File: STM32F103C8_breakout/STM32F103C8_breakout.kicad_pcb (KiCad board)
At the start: 2 copper layers, 49 parts, among them J1 Conn1x1Pin-PA0_WKUP, J10 Conn1x1Pin-PA9, J11 Conn1x1Pin-PA10, J12 Conn1x1Pin-PA11, J13 Conn1x1Pin-PA12, J14 Conn1x1Pin-PA13, J15 Conn1x1Pin-PA14, J16 Conn1x1Pin-PA15, J17 Conn1x1Pin-PC13-TAMPER-RTC, J18 Conn1x1Pin-PC14-OSC32_IN, J19 Conn1x1Pin-PC15-OSC32_OUT, J2 Conn1x1Pin-PA1, J20 Conn1x1Pin-VBAT, J21 Conn1x1Pin-NRST, J22 BOOT0, J23 Conn1x1Pin-VDD, J24 Conn1x1Pin-VDDA, J25 Conn1x1Pin-PB15, J26 Conn1x1Pin-PB14, J27 Conn1x1Pin-PB13, J28 Conn1x1Pin-PB12, J29 Conn1x1Pin-PB11, J3 Conn1x1Pin-PA2, J30 Conn1x1Pin-PB10, J31 Conn1x1Pin-PB9, J32 Conn1x1Pin-PB8, J33 Conn1x1Pin-PB7, J34 Conn1x1Pin-PB6, J35 Conn1x1Pin-PB5, J36 Conn1x1Pin-PB4, J37 Conn1x1Pin-PB3, J38 Conn1x1Pin-PB2, J39 Conn1x1Pin-PB1, J4 Conn1x1Pin-PA3, J40 Conn1x1Pin-PB0, J41 Conn1x1Pin-PC0_OSC_IN, J42 Conn1x1Pin-PD1_OSC_OUT, J43 Conn1x1Pin-VSSA, J44 Conn1x1Pin-VSS, J5 Conn1x1Pin-PA4, J6 Conn1x1Pin-PA5, J7 Conn1x1Pin-PA6, J8 Conn1x1Pin-PA7, J9 Conn1x1Pin-PA8, U1 STM32F103C8T6

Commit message: Added to Schematics
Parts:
- removed J20: Conn1x1Pin-VBAT, Connector_PinHeader_2.54mm:PinHeader_1x01_P2.54mm_Horizontal
- removed J21: Conn1x1Pin-NRST, Connector_PinHeader_2.54mm:PinHeader_1x01_P2.54mm_Horizontal
- removed J22: BOOT0, Connector_PinHeader_2.54mm:PinHeader_1x01_P2.54mm_Horizontal
- removed J23 (x3): Conn1x1Pin-VDD, Connector_PinHeader_2.54mm:PinHeader_1x01_P2.54mm_Horizontal
- removed J24: Conn1x1Pin-VDDA, Connector_PinHeader_2.54mm:PinHeader_1x01_P2.54mm_Horizontal
- removed J41: Conn1x1Pin-PC0_OSC_IN, Connector_PinHeader_2.54mm:PinHeader_1x01_P2.54mm_Horizontal
- removed J42: Conn1x1Pin-PD1_OSC_OUT, Connector_PinHeader_2.54mm:PinHeader_1x01_P2.54mm_Horizontal
- removed J43: Conn1x1Pin-VSSA, Connector_PinHeader_2.54mm:PinHeader_1x01_P2.54mm_Horizontal
- removed J44 (x3): Conn1x1Pin-VSS, Connector_PinHeader_2.54mm:PinHeader_1x01_P2.54mm_Horizontal
- removed U1: STM32F103C8T6, STM32F103C8T6:QFP50P900X900X160-48N
- added C1: 1μF, Capacitor_SMD:C_0805_2012Metric_Pad1.18x1.45mm_HandSolder, F.Cu at (178.4, 50.0)
- added C2: 100nF, Capacitor_SMD:C_0805_2012Metric_Pad1.18x1.45mm_HandSolder, F.Cu at (178.4, 53.0)
- added C3: 100nF, Capacitor_SMD:C_0805_2012Metric_Pad1.18x1.45mm_HandSolder, F.Cu at (178.4, 56.0)
- added C4: 20pF, Capacitor_SMD:C_0805_2012Metric_Pad1.18x1.45mm_HandSolder, F.Cu at (178.4, 59.0)
- added C5: 20pF, Capacitor_SMD:C_0805_2012Metric_Pad1.18x1.45mm_HandSolder, F.Cu at (178.4, 62.0)
- added FB1: FerriteBead_Small, Inductor_SMD:L_0805_2012Metric_Pad1.05x1.20mm_HandSolder, F.Cu at (178.4, 79.6)
- added JLINK/SWD1: ~, Connector_IDC:IDC-Header_2x10_P2.54mm_Vertical, F.Cu at (239.2, 71.8)
- added R1: 10kΩ, Resistor_SMD:R_0805_2012Metric_Pad1.20x1.40mm_HandSolder, F.Cu at (178.3, 65.0)
- added R2: 10kΩ, Resistor_SMD:R_0805_2012Metric_Pad1.20x1.40mm_HandSolder, F.Cu at (178.3, 67.9)
- added R3: 10kΩ, Resistor_SMD:R_0805_2012Metric_Pad1.20x1.40mm_HandSolder, F.Cu at (178.3, 70.9)
- added R5: 10kΩ, Resistor_SMD:R_0805_2012Metric_Pad1.20x1.40mm_HandSolder, F.Cu at (178.3, 73.8)
- added R6: 400Ω, Resistor_SMD:R_0805_2012Metric_Pad1.20x1.40mm_HandSolder, F.Cu at (178.3, 76.8)
- added Y1: 6 MHz Crystal, Crystal:Crystal_SMD_HC49-SD_HandSoldering, F.Cu at (227.0, 61.5)
- moved J17 107.2 mm to (139.5, 69.1), turned to 0 degrees
- moved J18 99.9 mm to (139.5, 73.7), turned to 0 degrees
- moved J31 96.1 mm to (152.9, 55.4), turned to 0 degrees
- moved J19 92.7 mm to (139.5, 78.3), turned to 0 degrees
- moved J30 92.7 mm to (152.9, 50.8), turned to 0 degrees
- moved J1 90.9 mm to (126.2, 50.8), turned to 0 degrees
- moved J32 90.4 mm to (152.9, 59.9), turned to 0 degrees
- moved J2 85.1 mm to (126.2, 55.4), turned to 0 degrees
- moved J3 79.5 mm to (126.2, 59.9), turned to 0 degrees
- moved J33 79.5 mm to (152.9, 64.5), turned to 0 degrees
- moved J4 75.9 mm to (126.2, 64.5), turned to 0 degrees
- moved J28 75.1 mm to (139.5, 96.7), turned to 0 degrees
- moved J34 74.3 mm to (152.9, 69.1), turned to 0 degrees
- moved J5 72.1 mm to (126.2, 69.1), turned to 0 degrees
- moved J35 69.6 mm to (152.9, 73.7), turned to 0 degrees
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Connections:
- J14 pad 1: Net-(J14-Pin_1) -> /JTMS/SWDIO
- J15 pad 1: Net-(J15-Pin_1) -> /JTDI
- J16 pad 1: Net-(J16-Pin_1) -> /JTCK/SWCLK
- J36 pad 1: Net-(J36-Pin_1) -> /JNTRST
- J37 pad 1: Net-(J37-Pin_1) -> /JTDO

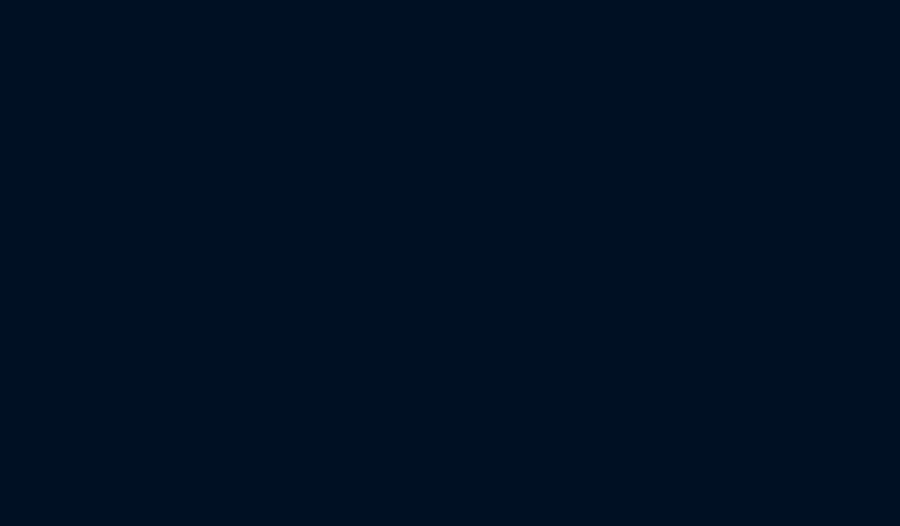
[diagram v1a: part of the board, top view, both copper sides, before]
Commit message: Updated Boot Switch from SPDT to Jumper Functionality
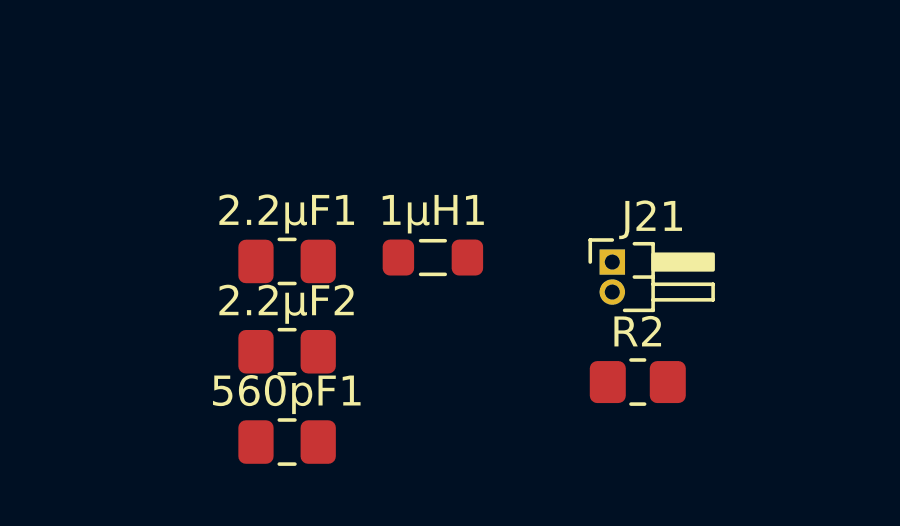
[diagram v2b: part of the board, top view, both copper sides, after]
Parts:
- added 1µH1: L_Small, Inductor_SMD:L_0805_2012Metric_Pad1.05x1.20mm_HandSolder, F.Cu at (184.3, 96.3)
- added 2.2µF1: C_Small_US, Capacitor_SMD:C_0805_2012Metric_Pad1.18x1.45mm_HandSolder, F.Cu at (179.4, 96.4)
- added 2.2µF2: C_Small_US, Capacitor_SMD:C_0805_2012Metric_Pad1.18x1.45mm_HandSolder, F.Cu at (179.4, 99.4)
- added 560pF1: C_Small_US, Capacitor_SMD:C_0805_2012Metric_Pad1.18x1.45mm_HandSolder, F.Cu at (179.4, 102.4)
- added J21: Conn_01x02_Pin, Connector_PinHeader_1.00mm:PinHeader_1x02_P1.00mm_Horizontal, F.Cu at (190.2, 96.4)
- added R2: 10kΩ, Resistor_SMD:R_0805_2012Metric_Pad1.20x1.40mm_HandSolder, F.Cu at (191.1, 100.4)
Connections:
- net /nRST renamed /RST_IN

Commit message: Worked on PCB Layout
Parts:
- removed J10: Conn1x1Pin-PA9, Connector_PinHeader_2.54mm:PinHeader_1x01_P2.54mm_Horizontal
- removed J11: Conn1x1Pin-PA10, Connector_PinHeader_2.54mm:PinHeader_1x01_P2.54mm_Horizontal
- removed J12: Conn1x1Pin-PA11, Connector_PinHeader_2.54mm:PinHeader_1x01_P2.54mm_Horizontal
- removed J13: Conn1x1Pin-PA12, Connector_PinHeader_2.54mm:PinHeader_1x01_P2.54mm_Horizontal
- removed J14: Conn1x1Pin-PA13, Connector_PinHeader_2.54mm:PinHeader_1x01_P2.54mm_Horizontal
- removed J15: Conn1x1Pin-PA14, Connector_PinHeader_2.54mm:PinHeader_1x01_P2.54mm_Horizontal
- removed J16: Conn1x1Pin-PA15, Connector_PinHeader_2.54mm:PinHeader_1x01_P2.54mm_Horizontal
- removed J17: Conn1x1Pin-PC13-TAMPER-RTC, Connector_PinHeader_2.54mm:PinHeader_1x01_P2.54mm_Horizontal
- removed J18: Conn1x1Pin-PC14-OSC32_IN, Connector_PinHeader_2.54mm:PinHeader_1x01_P2.54mm_Horizontal
- removed J19: Conn1x1Pin-PC15-OSC32_OUT, Connector_PinHeader_2.54mm:PinHeader_1x01_P2.54mm_Horizontal
- removed J25: Conn1x1Pin-PB15, Connector_PinHeader_2.54mm:PinHeader_1x01_P2.54mm_Horizontal
- removed J26: Conn1x1Pin-PB14, Connector_PinHeader_2.54mm:PinHeader_1x01_P2.54mm_Horizontal
- removed J27: Conn1x1Pin-PB13, Connector_PinHeader_2.54mm:PinHeader_1x01_P2.54mm_Horizontal
- removed J28: Conn1x1Pin-PB12, Connector_PinHeader_2.54mm:PinHeader_1x01_P2.54mm_Horizontal
- removed J29: Conn1x1Pin-PB11, Connector_PinHeader_2.54mm:PinHeader_1x01_P2.54mm_Horizontal
- removed J3: Conn1x1Pin-PA2, Connector_PinHeader_2.54mm:PinHeader_1x01_P2.54mm_Horizontal
- removed J30: Conn1x1Pin-PB10, Connector_PinHeader_2.54mm:PinHeader_1x01_P2.54mm_Horizontal
- removed J31: Conn1x1Pin-PB9, Connector_PinHeader_2.54mm:PinHeader_1x01_P2.54mm_Horizontal
- removed J32: Conn1x1Pin-PB8, Connector_PinHeader_2.54mm:PinHeader_1x01_P2.54mm_Horizontal
- removed J33: Conn1x1Pin-PB7, Connector_PinHeader_2.54mm:PinHeader_1x01_P2.54mm_Horizontal
- removed J34: Conn1x1Pin-PB6, Connector_PinHeader_2.54mm:PinHeader_1x01_P2.54mm_Horizontal
- removed J35: Conn1x1Pin-PB5, Connector_PinHeader_2.54mm:PinHeader_1x01_P2.54mm_Horizontal
- removed J36: Conn1x1Pin-PB4, Connector_PinHeader_2.54mm:PinHeader_1x01_P2.54mm_Horizontal
- removed J37: Conn1x1Pin-PB3, Connector_PinHeader_2.54mm:PinHeader_1x01_P2.54mm_Horizontal
- removed J38: Conn1x1Pin-PB2, Connector_PinHeader_2.54mm:PinHeader_1x01_P2.54mm_Horizontal
- removed J39: Conn1x1Pin-PB1, Connector_PinHeader_2.54mm:PinHeader_1x01_P2.54mm_Horizontal
- removed J4: Conn1x1Pin-PA3, Connector_PinHeader_2.54mm:PinHeader_1x01_P2.54mm_Horizontal
- removed J40: Conn1x1Pin-PB0, Connector_PinHeader_2.54mm:PinHeader_1x01_P2.54mm_Horizontal
- removed J5: Conn1x1Pin-PA4, Connector_PinHeader_2.54mm:PinHeader_1x01_P2.54mm_Horizontal
- removed J6: Conn1x1Pin-PA5, Connector_PinHeader_2.54mm:PinHeader_1x01_P2.54mm_Horizontal
- removed J7: Conn1x1Pin-PA6, Connector_PinHeader_2.54mm:PinHeader_1x01_P2.54mm_Horizontal
- removed J8: Conn1x1Pin-PA7, Connector_PinHeader_2.54mm:PinHeader_1x01_P2.54mm_Horizontal
- removed J9: Conn1x1Pin-PA8, Connector_PinHeader_2.54mm:PinHeader_1x01_P2.54mm_Horizontal
- added D1: WL-SMCC_0402, SMD_LED_GREEN:WL-SMCC_0402, F.Cu at (193.8, 149.1)
- added J20: USB-C, CONN_USBC:CONN_1054500101_MOL, F.Cu at (131.5, 87.7)
- added R7: 10kΩ, Resistor_SMD:R_0805_2012Metric_Pad1.20x1.40mm_HandSolder, F.Cu at (100.3, 29.4)
- added U1: STM32F103C8T6, STM32F103C8T6:QFP50P900X900X160-48N, F.Cu at (159.9, 98.0)
- added U2: BUCK_REG_3.3V, 3.3V_Buck:MLF-8_ML_MCH, F.Cu at (141.6, 87.5)
- added U3: GPTS203211B, Push_Button:SWITCH_03211B, F.Cu at (141.9, 101.4)
- J1: value Conn1x1Pin-PA0_WKUP -> Conn_01x18_Pin; footprint Connector_PinHeader_2.54mm:PinHeader_1x01_P2.54mm_Horizontal -> Connector_PinHeader_2.54mm:PinHeader_1x18_P2.54mm_Vertical
- J2: value Conn1x1Pin-PA1 -> Conn_01x14_Pin; footprint Connector_PinHeader_2.54mm:PinHeader_1x01_P2.54mm_Horizontal -> Connector_PinHeader_2.54mm:PinHeader_1x14_P2.54mm_Vertical
- J21: footprint Connector_PinHeader_1.00mm:PinHeader_1x02_P1.00mm_Horizontal -> Connector_PinHeader_2.54mm:PinHeader_1x02_P2.54mm_Vertical
- moved R2 107.0 mm to (85.1, 115.5)
- moved C3 91.5 mm to (87.9, 42.0)
- moved FB1 91.5 mm to (88.0, 65.7)
- moved C1 91.5 mm to (87.9, 36.0)
- moved C2 91.5 mm to (87.9, 39.0)
- moved R1 91.5 mm to (87.9, 51.0)
- moved R3 91.5 mm to (87.9, 57.0)
- moved J1 67.3 mm to (138.3, 117.0), turned to 90 degrees
- moved Y1 58.8 mm to (180.8, 97.9), turned to -90 degrees
- moved JLINK/SWD1 51.0 mm to (190.4, 86.5)
- moved 2.2µF1 49.1 mm to (130.3, 95.6)
- moved C4 46.4 mm to (185.2, 104.9), turned to -90 degrees
- moved R5 43.3 mm to (146.9, 103.7), turned to 180 degrees
- moved 1µH1 42.6 mm to (141.7, 94.3), turned to 180 degrees
- moved 560pF1 39.5 mm to (141.7, 90.7), turned to 180 degrees
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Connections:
- net /PowerSupply/USB_OUT_MCU_IN renamed /PowerSupply/Vdd
- J1 pad 1: Net-(J1-Pin_1) -> VDD
- J2 pad 1: Net-(J2-Pin_1) -> /PB9
- R2 pad 1: Net-(SW2-B) -> GNDREF
- R2 pad 2: Net-(U1-BOOT0) -> /BOOT_IN
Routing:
- net Net-(U1-PD0_OSC_IN): track 0.00 -> 32.7 mm, vias 0 -> 2
- net /BOOT_IN: track 0.00 -> 32.1 mm, vias 0 -> 1
- net /PB9: track 0.00 -> 24.8 mm
- net /PB11: track 0.00 -> 24.5 mm
- net /PC13: track 0.00 -> 23.6 mm
- net /PB8: track 0.00 -> 23.4 mm
- net /PB10: track 0.00 -> 23.2 mm
- net /RST_IN: track 0.00 -> 22.9 mm, vias 0 -> 1
- net /PC14: track 0.00 -> 22.4 mm
- net /PB2: track 0.00 -> 22.0 mm
- net Net-(U1-PD1_OSC_OUT): track 0.00 -> 21.9 mm
- net /PB7: track 0.00 -> 21.9 mm
- net /PC15: track 0.00 -> 21.1 mm
- net /PB12: track 0.00 -> 20.8 mm
- net /PB1: track 0.00 -> 20.7 mm
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- added copper zone on B.Cu, net (none)
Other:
- board outline added: 70.8 x 42.5 mm
- board text added: "gnd top, vdd bottom"

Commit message: Added any unsaved changes
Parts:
- moved FB1 71.6 mm to (151.8, 98.1), turned to 180 degrees
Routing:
- net /PowerSupply/GND: track 0.00 -> 19.6 mm
- net VDD: track 0.00 -> 6.34 mm, vias 0 -> 1
- added copper zone on F.Cu, net GNDREF
- added copper zone on B.Cu, net VDD
- removed copper zone on B.Cu, net (none)

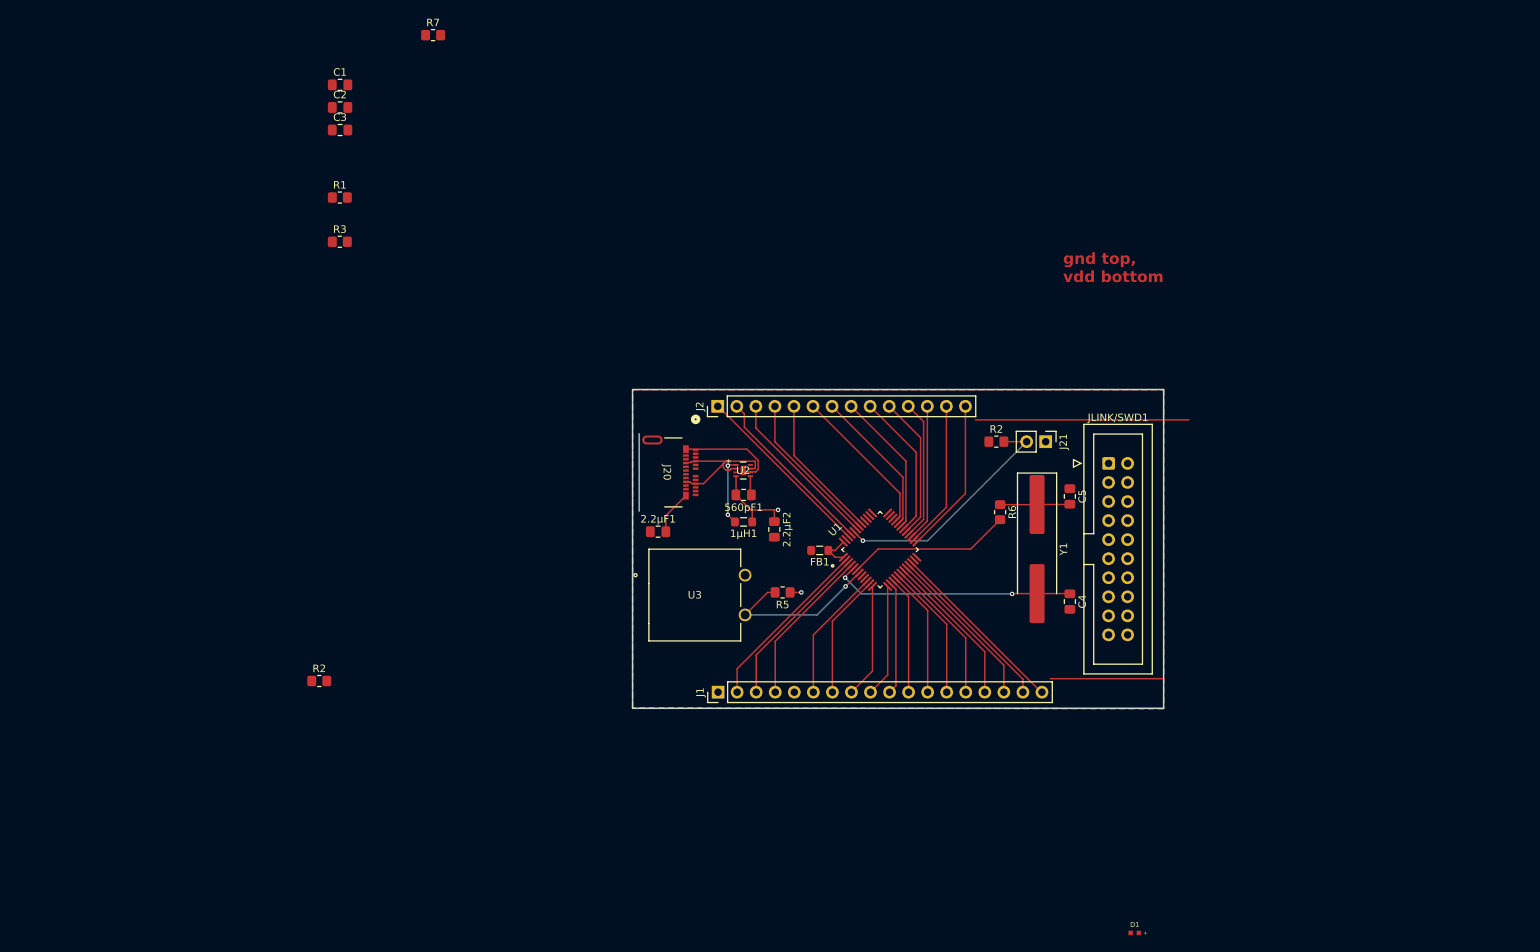
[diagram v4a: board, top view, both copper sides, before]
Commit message: Completed PCB Layoutx
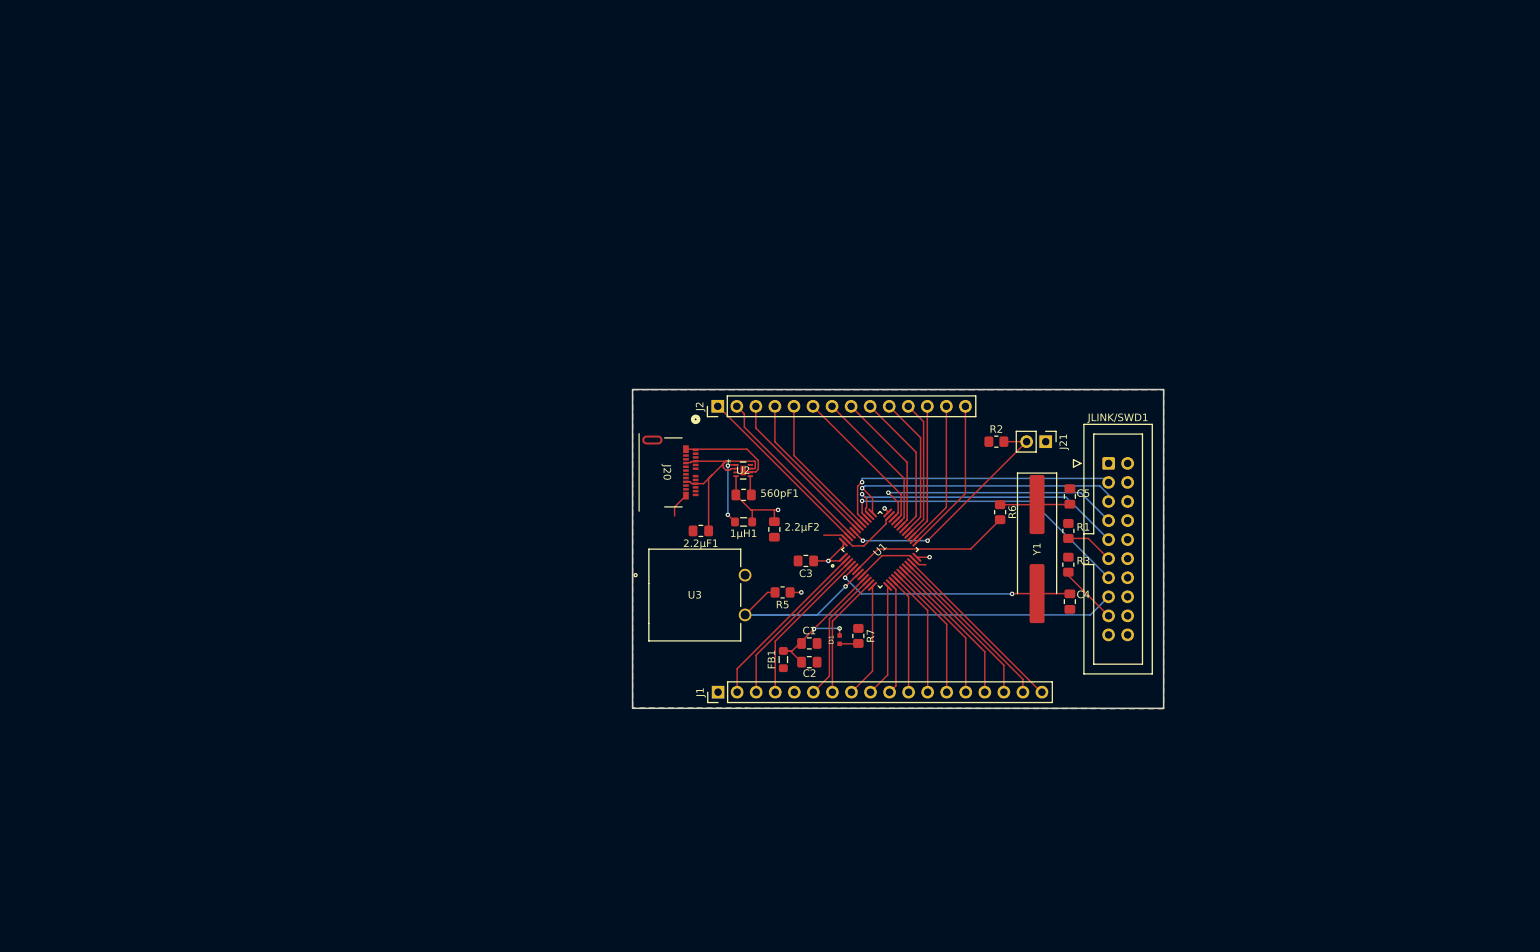
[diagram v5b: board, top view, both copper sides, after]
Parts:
- removed the R2 at (85.1, 115.5)
- moved R1 106.8 mm to (185.0, 95.5), turned to 90 degrees
- moved R3 106.2 mm to (185.0, 100.0), turned to 90 degrees
- moved R7 98.1 mm to (157.0, 109.5), turned to -90 degrees
- moved C1 97.3 mm to (150.5, 110.5)
- moved C2 96.9 mm to (150.5, 113.0)
- moved C3 84.6 mm to (150.0, 99.5), turned to 180 degrees
- moved D1 55.5 mm to (154.5, 110.0), turned to 90 degrees
- moved FB1 15.3 mm to (147.0, 112.7), turned to 90 degrees
- moved 2.2µF1 5.70 mm to (136.0, 95.5), turned to 180 degrees
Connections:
- 1µH1 pad 1: /PowerSupply/Vdd -> Vdd
- 2.2µF1 pad 2: /PowerSupply/GND -> GNDREF
- 2.2µF2 pad 1: /PowerSupply/Vdd -> Vdd
- 2.2µF2 pad 2: /PowerSupply/GND -> GNDREF
- 560pF1 pad 2: /PowerSupply/Vdd -> Vdd
- C3 pad 1: VDD -> Vdd
- FB1 pad 1: VDD -> Vdd
- J1 pad 1: VDD -> Vdd
- J20 pad A1: /PowerSupply/GND -> GNDREF
- J20 pad A12: /PowerSupply/GND -> GNDREF
- J20 pad B1: /PowerSupply/GND -> GNDREF
- J20 pad B12: /PowerSupply/GND -> GNDREF
- J21 pad 1: VDD -> Vdd
- JLINK/SWD1 pad 1: VDD -> Vdd
- R5 pad 1: VDD -> Vdd
- U1 pad 1: VDD -> Vdd
- U1 pad 24: VDD -> Vdd
- U1 pad 36: VDD -> Vdd
- U1 pad 48: VDD -> Vdd
- U2 pad 4: /PowerSupply/Vdd -> Vdd
- U2 pad 6: /PowerSupply/GND -> GNDREF
- U2 pad 8: /PowerSupply/GND -> GNDREF
- U2 pad 9: /PowerSupply/GND -> GNDREF
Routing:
- net /RST_IN: track 22.8 -> 72.2 mm
- net /JTDO: track 0.00 -> 39.7 mm, vias 0 -> 1
- net /JNTRST: track 0.00 -> 39.4 mm, vias 0 -> 1
- net /JTCK/SWCLK: track 0.00 -> 38.9 mm, vias 0 -> 1
- net GNDREF: track 0.00 -> 38.6 mm
- net /JTDI: track 0.00 -> 38.4 mm, vias 0 -> 1
- net /JTMS/SWDIO: track 0.00 -> 35.1 mm, vias 0 -> 1
- net Vdd: track 0.00 -> 23.6 mm, vias 0 -> 5
- net Net-(U1-VDDA): track 0.00 -> 22.3 mm, vias 0 -> 2
- net /PowerSupply/GND: track 19.6 -> 0.00 mm
- net /PowerSupply/Vdd: track 12.2 -> 0.00 mm, vias 1 -> 0
- net Net-(JLINK/SWD1-DBGRQ): track 0.00 -> 8.04 mm
- net /PowerSupply/V_IN: track 20.7 -> 28.3 mm
- net Net-(JLINK/SWD1-RTCK): track 0.00 -> 6.48 mm
- net VDD: track 6.34 -> 0.00 mm, vias 1 -> 0
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- added copper zone on B.Cu, net Vdd
- removed copper zone on B.Cu, net VDD
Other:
- board text removed: "gnd top, vdd bottom"
